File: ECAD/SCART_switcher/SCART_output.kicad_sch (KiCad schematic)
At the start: 9 parts, among them J14 RCA Right, J3 RCA Left, Q3 BC847

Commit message: Progressed ECAD.
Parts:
- renumbered J3 to J2, J14 to J3
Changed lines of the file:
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@@
   (symbol (lib_id "power:+12V") (at 118.11 67.31 0) (unit 1)
     (in_bom yes) (on_board yes) (dnp no) (fields_autoplaced)
-    (property "Reference" "#PWR021" (at 118.11 71.12 0)
+    (property "Reference" "#PWR023" (at 118.11 71.12 0)
       (effects (font (size 1.27 1.27)) hide)
     )
@@
       (project "SCART_switcher"
         (path "/8cd08eb5-4755-4ef5-8eeb-77fd9974b180/6562ea38-5963-42b2-a0ef-a4a12a4c652f"
-          (reference "#PWR021") (unit 1)
+          (reference "#PWR023") (unit 1)
         )
       )
@@
   (symbol (lib_id "Connector:Conn_Coaxial") (at 102.87 146.05 0) (unit 1)
     (in_bom yes) (on_board yes) (dnp no) (fields_autoplaced)
-    (property "Reference" "J14" (at 106.68 145.0732 0)
+    (property "Reference" "J3" (at 106.68 145.0732 0)
       (effects (font (size 1.27 1.27)) (justify left))
     )
@@
       (project "SCART_switcher"
         (path "/8cd08eb5-4755-4ef5-8eeb-77fd9974b180/6562ea38-5963-42b2-a0ef-a4a12a4c652f"
-          (reference "J14") (unit 1)
+          (reference "J3") (unit 1)
         )
       )
@@
         )
         (path "/8cd08eb5-4755-4ef5-8eeb-77fd9974b180/6562ea38-5963-42b2-a0ef-a4a12a4c652f"
-          (reference "#PWR029") (unit 1)
+          (reference "#PWR031") (unit 1)
         )
       )
@@
         )
         (path "/8cd08eb5-4755-4ef5-8eeb-77fd9974b180/6562ea38-5963-42b2-a0ef-a4a12a4c652f"
-          (reference "#PWR026") (unit 1)
+          (reference "#PWR028") (unit 1)
         )
       )
@@
         )
         (path "/8cd08eb5-4755-4ef5-8eeb-77fd9974b180/6562ea38-5963-42b2-a0ef-a4a12a4c652f"
+          (reference "J4") (unit 1)
+        )
+      )
+    )
+  )
+  (symbol (lib_id "power:+5V") (at 85.09 69.85 0) (unit 1)
+    (in_bom yes) (on_board yes) (dnp no) (fields_autoplaced)
+    (property "Reference" "#PWR?" (at 85.09 73.66 0)
+      (effects (font (size 1.27 1.27)) hide)
+    )
+    (property "Value" "+5V" (at 85.09 64.77 0)
+      (effects (font (size 1.27 1.27)))
+    )
+    (property "Footprint" "" (at 85.09 69.85 0)
+      (effects (font (size 1.27 1.27)) hide)
+    )
+    (property "Datasheet" "" (at 85.09 69.85 0)
+      (effects (font (size 1.27 1.27)) hide)
+    )
+    (pin "1")
+    (instances
+      (project "SCART_switcher"
+        (path "/8cd08eb5-4755-4ef5-8eeb-77fd9974b180/6e53f4c9-ed59-4c5d-ac8d-a66f0d353ca7"
+          (reference "#PWR?") (unit 1)
+        )
+        (path "/8cd08eb5-4755-4ef5-8eeb-77fd9974b180/8ea6db35-25d0-43bc-9de5-3ca23502dcdc"
+          (reference "#PWR?") (unit 1)
+        )
+        (path "/8cd08eb5-4755-4ef5-8eeb-77fd9974b180/272a4677-3ef2-418e-abc5-b29f59e726f9"
+          (reference "#PWR?") (unit 1)
+        )
+        (path "/8cd08eb5-4755-4ef5-8eeb-77fd9974b180/56b7edd2-65bf-4844-b6bd-3868b6562f83"
+          (reference "#PWR?") (unit 1)
+        )
+        (path "/8cd08eb5-4755-4ef5-8eeb-77fd9974b180/a066fdde-5f40-4269-95c1-258d611fd7cb"
+          (reference "#PWR?") (unit 1)
+        )
+        (path "/8cd08eb5-4755-4ef5-8eeb-77fd9974b180/ec158eb5-f3e0-409c-b64c-a90e3358941f"
+          (reference "#PWR?") (unit 1)
+        )
+        (path "/8cd08eb5-4755-4ef5-8eeb-77fd9974b180/6c53b757-b2e6-4d60-b760-4a4a0f832c07"
+          (reference "#PWR?") (unit 1)
+        )
+        (path "/8cd08eb5-4755-4ef5-8eeb-77fd9974b180/0223a704-ac47-44ed-9ba1-f418acceedb3"
+          (reference "#PWR?") (unit 1)
+        )
+        (path "/8cd08eb5-4755-4ef5-8eeb-77fd9974b180/2ffa7ecd-d29d-4261-a577-43650ca26099"
+          (reference "#PWR?") (unit 1)
+        )
+        (path "/8cd08eb5-4755-4ef5-8eeb-77fd9974b180/f71a1287-269d-4354-9179-cb80a7e1dbca"
+          (reference "#PWR?") (unit 1)
+        )
+        (path "/8cd08eb5-4755-4ef5-8eeb-77fd9974b180/6562ea38-5963-42b2-a0ef-a4a12a4c652f"
+          (reference "#PWR019") (unit 1)
+        )
+      )
+    )
+  )
+  (symbol (lib_id "Connector:Conn_Coaxial") (at 102.87 128.27 0) (unit 1)
+    (in_bom yes) (on_board yes) (dnp no) (fields_autoplaced)
+    (property "Reference" "J2" (at 106.68 127.2932 0)
+      (effects (font (size 1.27 1.27)) (justify left))
+    )
+    (property "Value" "RCA Left" (at 106.68 129.8332 0)
+      (effects (font (size 1.27 1.27)) (justify left))
+    )
+    (property "Footprint" "Connector_RCA:RCA_Vertical" (at 102.87 128.27 0)
+      (effects (font (size 1.27 1.27)) hide)
+    )
+    (property "Datasheet" " ~" (at 102.87 128.27 0)
+      (effects (font (size 1.27 1.27)) hide)
+    )
+    (pin "1")
+    (pin "2")
+    (instances
+      (project "SCART_switcher"
+        (path "/8cd08eb5-4755-4ef5-8eeb-77fd9974b180/6562ea38-5963-42b2-a0ef-a4a12a4c652f"
           (reference "J2") (unit 1)
         )
@@
     )
   )
-  (symbol (lib_id "power:+5V") (at 85.09 69.85 0) (unit 1)
-    (in_bom yes) (on_board yes) (dnp no) (fields_autoplaced)
-    (property "Reference" "#PWR?" (at 85.09 73.66 0)
-      (effects (font (size 1.27 1.27)) hide)
-    )
-    (property "Value" "+5V" (at 85.09 64.77 0)
-      (effects (font (size 1.27 1.27)))
-    )
-    (property "Footprint" "" (at 85.09 69.85 0)
-      (effects (font (size 1.27 1.27)) hide)
-    )
-    (property "Datasheet" "" (at 85.09 69.85 0)
-      (effects (font (size 1.27 1.27)) hide)
-    )
-    (pin "1")
-    (instances
-      (project "SCART_switcher"
-        (path "/8cd08eb5-4755-4ef5-8eeb-77fd9974b180/6e53f4c9-ed59-4c5d-ac8d-a66f0d353ca7"
-          (reference "#PWR?") (unit 1)
-        )
-        (path "/8cd08eb5-4755-4ef5-8eeb-77fd9974b180/8ea6db35-25d0-43bc-9de5-3ca23502dcdc"
-          (reference "#PWR?") (unit 1)
-        )
-        (path "/8cd08eb5-4755-4ef5-8eeb-77fd9974b180/272a4677-3ef2-418e-abc5-b29f59e726f9"
-          (reference "#PWR?") (unit 1)
-        )
-        (path "/8cd08eb5-4755-4ef5-8eeb-77fd9974b180/56b7edd2-65bf-4844-b6bd-3868b6562f83"
-          (reference "#PWR?") (unit 1)
-        )
-        (path "/8cd08eb5-4755-4ef5-8eeb-77fd9974b180/a066fdde-5f40-4269-95c1-258d611fd7cb"
-          (reference "#PWR?") (unit 1)
-        )
-        (path "/8cd08eb5-4755-4ef5-8eeb-77fd9974b180/ec158eb5-f3e0-409c-b64c-a90e3358941f"
-          (reference "#PWR?") (unit 1)
-        )
-        (path "/8cd08eb5-4755-4ef5-8eeb-77fd9974b180/6c53b757-b2e6-4d60-b760-4a4a0f832c07"
-          (reference "#PWR?") (unit 1)
-        )
-        (path "/8cd08eb5-4755-4ef5-8eeb-77fd9974b180/0223a704-ac47-44ed-9ba1-f418acceedb3"
-          (reference "#PWR?") (unit 1)
-        )
-        (path "/8cd08eb5-4755-4ef5-8eeb-77fd9974b180/2ffa7ecd-d29d-4261-a577-43650ca26099"
-          (reference "#PWR?") (unit 1)
-        )
-        (path "/8cd08eb5-4755-4ef5-8eeb-77fd9974b180/f71a1287-269d-4354-9179-cb80a7e1dbca"
-          (reference "#PWR?") (unit 1)
-        )
-        (path "/8cd08eb5-4755-4ef5-8eeb-77fd9974b180/6562ea38-5963-42b2-a0ef-a4a12a4c652f"
-          (reference "#PWR019") (unit 1)
-        )
-      )
-    )
-  )
-  (symbol (lib_id "Connector:Conn_Coaxial") (at 102.87 128.27 0) (unit 1)
-    (in_bom yes) (on_board yes) (dnp no) (fields_autoplaced)
-    (property "Reference" "J3" (at 106.68 127.2932 0)
-      (effects (font (size 1.27 1.27)) (justify left))
-    )
-    (property "Value" "RCA Left" (at 106.68 129.8332 0)
-      (effects (font (size 1.27 1.27)) (justify left))
-    )
-    (property "Footprint" "Connector_RCA:RCA_Vertical" (at 102.87 128.27 0)
-      (effects (font (size 1.27 1.27)) hide)
-    )
-    (property "Datasheet" " ~" (at 102.87 128.27 0)
-      (effects (font (size 1.27 1.27)) hide)
-    )
-    (pin "1")
-    (pin "2")
-    (instances
-      (project "SCART_switcher"
-        (path "/8cd08eb5-4755-4ef5-8eeb-77fd9974b180/6562ea38-5963-42b2-a0ef-a4a12a4c652f"
-          (reference "J3") (unit 1)
-        )
-      )
-    )
-  )
   (symbol (lib_id "power:GND") (at 118.11 85.09 0) (unit 1)
     (in_bom yes) (on_board yes) (dnp no) (fields_autoplaced)
@@
         )
         (path "/8cd08eb5-4755-4ef5-8eeb-77fd9974b180/6562ea38-5963-42b2-a0ef-a4a12a4c652f"
-          (reference "#PWR022") (unit 1)
+          (reference "#PWR024") (unit 1)
         )
       )
@@
         )
         (path "/8cd08eb5-4755-4ef5-8eeb-77fd9974b180/6562ea38-5963-42b2-a0ef-a4a12a4c652f"
-          (reference "#PWR023") (unit 1)
+          (reference "#PWR025") (unit 1)
         )
       )
@@
         )
         (path "/8cd08eb5-4755-4ef5-8eeb-77fd9974b180/6562ea38-5963-42b2-a0ef-a4a12a4c652f"
-          (reference "#PWR0884") (unit 1)
+          (reference "#PWR022") (unit 1)
         )
       )
@@
         )
         (path "/8cd08eb5-4755-4ef5-8eeb-77fd9974b180/6562ea38-5963-42b2-a0ef-a4a12a4c652f"
-          (reference "#PWR027") (unit 1)
+          (reference "#PWR029") (unit 1)
         )
       )
@@
         )
         (path "/8cd08eb5-4755-4ef5-8eeb-77fd9974b180/6562ea38-5963-42b2-a0ef-a4a12a4c652f"
-          (reference "#PWR030") (unit 1)
+          (reference "#PWR021") (unit 1)
         )
       )
@@
         )
         (path "/8cd08eb5-4755-4ef5-8eeb-77fd9974b180/6562ea38-5963-42b2-a0ef-a4a12a4c652f"
-          (reference "#PWR028") (unit 1)
+          (reference "#PWR030") (unit 1)
         )
       )
@@
         )
         (path "/8cd08eb5-4755-4ef5-8eeb-77fd9974b180/6562ea38-5963-42b2-a0ef-a4a12a4c652f"
-          (reference "#PWR024") (unit 1)
+          (reference "#PWR026") (unit 1)
         )
       )
@@
         )
         (path "/8cd08eb5-4755-4ef5-8eeb-77fd9974b180/6562ea38-5963-42b2-a0ef-a4a12a4c652f"
-          (reference "#PWR025") (unit 1)
-        )
-      )
+          (reference "#PWR027") (unit 1)
+        )
+      )

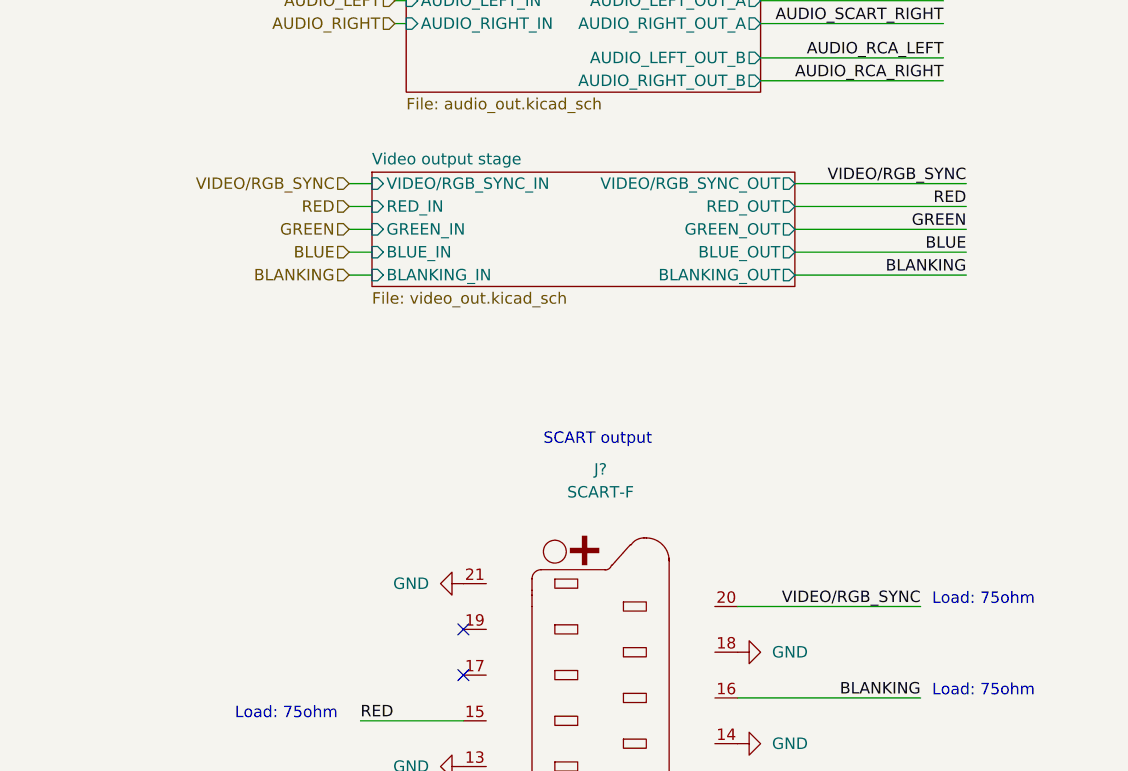
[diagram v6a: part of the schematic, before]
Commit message: ERC fixes.
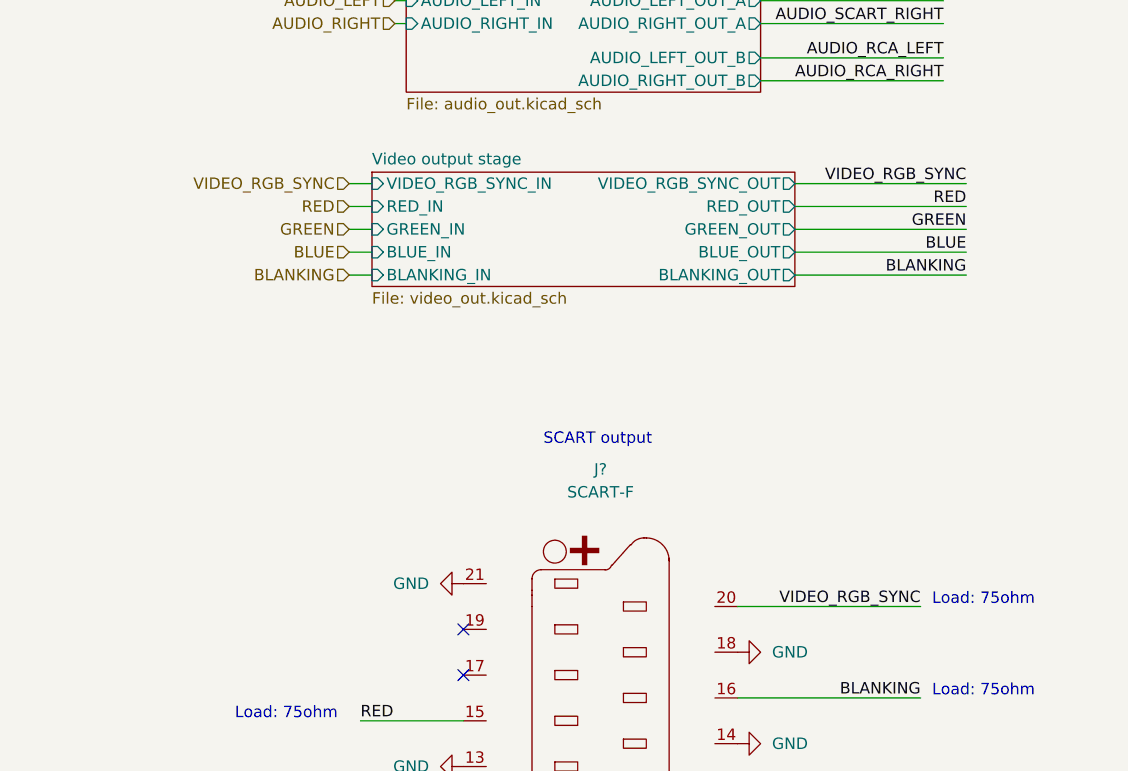
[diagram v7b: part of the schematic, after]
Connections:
- net VIDEO/RGB_SYNC renamed VIDEO_RGB_SYNC
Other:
- sheet Video output stage ports: added VIDEO_RGB_SYNC_IN, VIDEO_RGB_SYNC_OUT; removed VIDEO/RGB_SYNC_IN, VIDEO/RGB_SYNC_OUT
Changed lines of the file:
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@@
     (effects (font (size 1.27 1.27)) (justify right bottom))
   )
-  (label "VIDEO{slash}RGB_SYNC" (at 261.62 54.61 180) (fields_autoplaced)
+  (label "VIDEO_RGB_SYNC" (at 261.62 54.61 180) (fields_autoplaced)
     (effects (font (size 1.27 1.27)) (justify right bottom))
   )
@@
     (effects (font (size 1.27 1.27)) (justify left bottom))
   )
-  (label "VIDEO{slash}RGB_SYNC" (at 256.54 101.6 180) (fields_autoplaced)
+  (label "VIDEO_RGB_SYNC" (at 256.54 101.6 180) (fields_autoplaced)
     (effects (font (size 1.27 1.27)) (justify right bottom))
   )
@@
     (effects (font (size 1.27 1.27)) (justify right))
   )
-  (hierarchical_label "VIDEO{slash}RGB_SYNC" (shape input) (at 193.04 54.61 180) (fields_autoplaced)
+  (hierarchical_label "VIDEO_RGB_SYNC" (shape input) (at 193.04 54.61 180) (fields_autoplaced)
     (effects (font (size 1.27 1.27)) (justify right))
   )
@@
       (effects (font (size 1.27 1.27)) (justify left top))
     )
-    (pin "VIDEO{slash}RGB_SYNC_IN" input (at 195.58 54.61 180)
-      (effects (font (size 1.27 1.27)) (justify left))
-    )
     (pin "RED_IN" input (at 195.58 57.15 180)
       (effects (font (size 1.27 1.27)) (justify left))
@@
       (effects (font (size 1.27 1.27)) (justify left))
     )
-    (pin "VIDEO{slash}RGB_SYNC_OUT" output (at 242.57 54.61 0)
-      (effects (font (size 1.27 1.27)) (justify right))
-    )
     (pin "BLUE_OUT" output (at 242.57 62.23 0)
       (effects (font (size 1.27 1.27)) (justify right))
@@
       (effects (font (size 1.27 1.27)) (justify right))
     )
+    (pin "VIDEO_RGB_SYNC_IN" input (at 195.58 54.61 180)
+      (effects (font (size 1.27 1.27)) (justify left))
+    )
+    (pin "VIDEO_RGB_SYNC_OUT" output (at 242.57 54.61 0)
+      (effects (font (size 1.27 1.27)) (justify right))
+    )

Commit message: Progressed ECAD. Error fixing and cleanup.
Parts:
- removed C2: 100nC, Capacitor_SMD:C_0805_2012Metric_Pad1.18x1.45mm_HandSolder, symbol Device:C
- removed R6: 10kR, Resistor_SMD:R_0805_2012Metric_Pad1.20x1.40mm_HandSolder, symbol Device:R
- removed U?: 74AHC1G04, Package_TO_SOT_SMD:SOT-23-5, symbol 74xGxx:74AHC1G04
- added Q?: BC857, Package_TO_SOT_SMD:SOT-23, symbol Transistor_BJT:BC857
- added R? (x2): 47kR, Resistor_SMD:R_0805_2012Metric_Pad1.20x1.40mm_HandSolder, symbol Device:R
- added R?: 10kR, Resistor_SMD:R_0805_2012Metric_Pad1.20x1.40mm_HandSolder, symbol Device:R
- renumbered R8 to R10
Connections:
- net +12V: now also Q?.2 (E)
- net GND: now also R?.2
- net OUT_ACTIVE: now also R?.1
- net at Q3.1 (B): now also R?.2
- net at Q3.3 (C), R7.2: now also R?.1; no longer R10.1
- new net: Q?.1 (B), R?.2
- new net: Q?.3 (C), R10.1, R?.1
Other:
- note removed: "RCA output"
- moved on the sheet: Q3, R10, R7
